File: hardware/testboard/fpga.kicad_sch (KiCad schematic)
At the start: 66 parts, among them J801 Conn_01x06, SW801 Button, U801 SST26VF023BA, U802 SN74ALVC164245, U803 ICE40HX4K-TQ144, U804 SN74ALVC164245, U805 SN74ALVC164245, U806 SN74ALVC164245, U807 SN74ALVC164245, U808 SN74LVC07, U809 74AHCT04, U810 SN74LVC07

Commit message: testboard - schematic and route done
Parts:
- added C1: 4.7uF, Capacitor_SMD:C_0603_1608Metric, symbol Device:C
- added U1: ~, 68040:DACMOD, symbol 68040:DACMOD
- added U2: MAX98306 Amp, 68040:AMP, symbol 68040:AMP
- SW801: value Button -> BUTTON
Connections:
- net +3.3V: now also U810.13, C1.1, U1.1 (VIN), U2.1 (V_{DD})
- net A10: now also U806.23 (2B8); no longer U806.2 (1B1)
- net A11: now also U806.22 (2B7); no longer U806.3 (1B2)
- net A12: now also U806.20 (2B6); no longer U806.5 (1B3)
- net A13: now also U806.19 (2B5); no longer U806.6 (1B4)
- net A14: now also U806.17 (2B4); no longer U806.8 (1B5)
- net A15: now also U806.14 (2B2); no longer U806.11 (1B7)
- net A16: now also U806.16 (2B3); no longer U806.9 (1B6)
- net A17: now also U806.13 (2B1); no longer U806.12 (1B8)
- net A18: now also U806.11 (1B7); no longer U806.14 (2B2)
- net A19: now also U806.12 (1B8); no longer U806.13 (2B1)
- net A20: now also U806.8 (1B5); no longer U806.17 (2B4)
- net A21: now also U806.5 (1B3); no longer U806.20 (2B6)
- net A23: now also U806.9 (1B6); no longer U806.16 (2B3)
- net A25: now also U806.6 (1B4); no longer U806.19 (2B5)
- net A8: now also U806.2 (1B1); no longer U806.23 (2B8)
- net A9: now also U806.3 (1B2); no longer U806.22 (2B7)
- net BCLK: now also U803.94 (IOR_141_GBIN2); no longer U803.20 (IOL_13B_GBIN7)
- net D0: now also U805.6 (1B4); no longer U805.23 (2B8)
- net D1: now also U805.3 (1B2); no longer U805.22 (2B7)
- net D10: now also U805.16 (2B3); no longer U805.9 (1B6)
- net D11: now also U805.17 (2B4); no longer U805.8 (1B5)
- net D12: now also U805.19 (2B5); no longer U805.6 (1B4)
- net D13: now also U805.20 (2B6); no longer U805.5 (1B3)
- net D14: now also U805.22 (2B7); no longer U805.3 (1B2)
- net D15: now also U805.23 (2B8); no longer U805.2 (1B1)
- net D2: now also U805.8 (1B5); no longer U805.20 (2B6)
- net D3: now also U805.2 (1B1); no longer U805.19 (2B5)
- net D4: now also U805.5 (1B3); no longer U805.17 (2B4)
- net D5: now also U805.9 (1B6); no longer U805.16 (2B3)
- net D6: now also U805.11 (1B7); no longer U805.14 (2B2)
- net D7: now also U805.12 (1B8); no longer U805.13 (2B1)
- net D8: now also U805.13 (2B1); no longer U805.12 (1B8)
- net D9: now also U805.14 (2B2); no longer U805.11 (1B7)
- net FPGA_BTN: now also U803.93 (IOR_140_GBIN3); no longer U803.55 (IOB_91)
- net FPGA_LED: now also U803.95 (IOR_144), U808.9; no longer U803.52 (IOB_82_GBIN4), U810.11
- net GND: now also C1.2, U1.2 (GND), U2.2 (GND)
- net LV.A10: now also U803.29 (IOL_23B), U806.26 (2A8); no longer U803.10 (IOL_5B), U806.47 (1A1)
- net LV.A11: now also U803.28 (IOL_23A), U806.27 (2A7); no longer U803.11 (IOL_8A), U806.46 (1A2)
- net LV.A12: now also U803.26 (IOL_18B), U806.29 (2A6); no longer U803.12 (IOL_8B), U806.44 (1A3)
- net LV.A13: now also U803.25 (IOL_18A), U806.30 (2A5); no longer U803.15 (IOL_10A), U806.43 (1A4)
- net LV.A14: now also U803.24 (IOL_17B), U806.32 (2A4); no longer U803.16 (IOL_10B), U806.41 (1A5)
- net LV.A15: now also U803.22 (IOL_14B), U806.35 (2A2); no longer U803.18 (IOL_12B), U806.38 (1A7)
- net LV.A16: now also U803.23 (IOL_17A), U806.33 (2A3); no longer U803.17 (IOL_12A), U806.40 (1A6)
- net LV.A17: now also U803.21 (IOL_14A_GBIN6), U806.36 (2A1); no longer U803.19 (IOL_13A), U806.37 (1A8)
- net LV.A18: now also U803.18 (IOL_12B), U806.38 (1A7); no longer U803.22 (IOL_14B), U806.35 (2A2)
- net LV.A19: now also U803.19 (IOL_13A), U806.37 (1A8); no longer U803.21 (IOL_14A_GBIN6), U806.36 (2A1)
- net LV.A20: now also U803.16 (IOL_10B), U806.41 (1A5); no longer U803.24 (IOL_17B), U806.32 (2A4)
- net LV.A21: now also U803.12 (IOL_8B), U806.44 (1A3); no longer U803.26 (IOL_18B), U806.29 (2A6)
- net LV.A23: now also U803.17 (IOL_12A), U806.40 (1A6); no longer U803.23 (IOL_17A), U806.33 (2A3)
- net LV.A25: now also U803.15 (IOL_10A), U806.43 (1A4); no longer U803.25 (IOL_18A), U806.30 (2A5)
- net LV.A8: now also U803.10 (IOL_5B), U806.47 (1A1); no longer U803.29 (IOL_23B), U806.26 (2A8)
- net LV.A9: now also U803.11 (IOL_8A), U806.46 (1A2); no longer U803.28 (IOL_23A), U806.27 (2A7)
- net LV_68150_CS: now also U803.104 (IOR_164); no longer U803.44 (IOB_72)
- net LV_AVEC: now also U803.107 (IOR_167); no longer U803.42 (IOB_64)
- net LV_COM_CS: now also U803.102 (IOR_161); no longer U803.43 (IOB_71)
- net LV_COM_IACK: now also U803.105 (IOR_165); no longer U803.39 (IOB_61)
- net LV_D0: now also U803.138 (IOT_216), U805.43 (1A4); no longer U803.9 (IOL_5A), U805.26 (2A8)
- net LV_D1: now also U803.136 (IOT_214), U805.46 (1A2); no longer U803.8 (IOL_4B), U805.27 (2A7)
- net LV_D10: now also U803.2 (IOL_2B), U805.33 (2A3); no longer U803.141 (IOT_219), U805.40 (1A6)
- net LV_D11: now also U803.3 (IOL_3A), U805.32 (2A4); no longer U803.139 (IOT_217), U805.41 (1A5)
- net LV_D12: now also U803.4 (IOL_3B), U805.30 (2A5); no longer U803.138 (IOT_216), U805.43 (1A4)
- net LV_D13: now also U803.7 (IOL_4A), U805.29 (2A6); no longer U803.137 (IOT_215), U805.44 (1A3)
- net LV_D14: now also U803.8 (IOL_4B), U805.27 (2A7); no longer U803.136 (IOT_214), U805.46 (1A2)
- net LV_D15: now also U803.9 (IOL_5A), U805.26 (2A8); no longer U803.135 (IOT_213), U805.47 (1A1)
- net LV_D2: now also U803.139 (IOT_217), U805.41 (1A5); no longer U803.7 (IOL_4A), U805.29 (2A6)
- net LV_D3: now also U803.135 (IOT_213), U805.47 (1A1); no longer U803.4 (IOL_3B), U805.30 (2A5)
- net LV_D4: now also U803.137 (IOT_215), U805.44 (1A3); no longer U803.3 (IOL_3A), U805.32 (2A4)
- net LV_D5: now also U803.141 (IOT_219), U805.40 (1A6); no longer U803.2 (IOL_2B), U805.33 (2A3)
- net LV_D6: now also U803.142 (IOT_220), U805.38 (1A7); no longer U803.1 (IOL_2A), U805.35 (2A2)
- net LV_D7: now also U803.143 (IOT_221), U805.37 (1A8); no longer U803.144 (IOT_222), U805.36 (2A1)
- net LV_D8: now also U803.144 (IOT_222), U805.36 (2A1); no longer U803.143 (IOT_221), U805.37 (1A8)
- net LV_D9: now also U803.1 (IOL_2A), U805.35 (2A2); no longer U803.142 (IOT_220), U805.38 (1A7)
- net LV_RAM_CS: now also U803.106 (IOR_166); no longer U803.41 (IOB_63)
- net LV_R/~{W}: now also U803.42 (IOB_64)
- net LV_SIZ0: now also U803.43 (IOB_71)
- net LV_SIZ1: now also U803.44 (IOB_72)
- net LV_TM0: now also U803.41 (IOB_63)
- net LV_TM1: now also U803.39 (IOB_61)
- net LV_TM2: now also U803.38 (IOB_57)
- net LV_TT0: now also U803.49 (IOB_81_GBIN5)
- net LV_TT1: now also U803.48 (IOB_80)
- net LV_~{68150_DS}: now also U803.56 (IOB_94)
- net LV_~{COM_IRQ}: now also U802.29 (2A6), U803.55 (IOB_91); no longer U802.33 (2A3)
- net LV_~{DSACK0}: now also U803.96 (IOR_146), U808.11; no longer U803.101 (IOR_160), U808.9
- net LV_~{DSACK1}: now also U803.97 (IOR_147), U808.13; no longer U803.102 (IOR_161), U808.11
- net LV_~{IPL0}: now also U803.98 (IOR_148); no longer U803.105 (IOR_165)
- net LV_~{IPL1}: now also U803.99 (IOR_152); no longer U803.106 (IOR_166)
- net LV_~{IPL2}: now also U803.101 (IOR_160); no longer U803.107 (IOR_167)
- net LV_~{RST}: now also U802.27 (2A7), U803.52 (IOB_82_GBIN4); no longer U802.30 (2A5), U803.48 (IOB_80)
- net LV_~{TA}: now also U803.34 (IOL_25B), U810.11; no longer U803.104 (IOR_164), U808.13
- net LV_~{TBI}: now also U803.31 (IOL_24A)
- net LV_~{TCI}: now also U803.32 (IOL_24B)
- net LV_~{TEA}: now also U803.33 (IOL_25A)
- net LV_~{TIP}: now also U803.47 (IOB_79)
- net LV_~{TS}: now also U803.45 (IOB_73)
- net ~{COM_IRQ}: now also U802.20 (2B6); no longer U802.16 (2B3)
- net ~{DSACK0}: now also U808.10; no longer U808.8
- net ~{DSACK1}: now also U808.12; no longer U808.10
- net ~{RST}: now also U802.22 (2B7); no longer U802.19 (2B5)
- net ~{TA}: now also U810.10; no longer U808.12
- net at D803.1 (K): now also U808.8; no longer U810.10
- net SND_BCLK: now reaches U803.60 (IOB_95)
- net SND_BCLK: now also U1.5 (BCK)
- net SND_DOUT: now reaches U803.61 (IOB_96)
- net SND_DOUT: now also U1.4 (DIN)
- net SND_LRCLK: now reaches U803.62 (IOB_102)
- net SND_LRCLK: now also U1.3 (LRCLK)
- net ~{FPGA_RDY} renamed ~{FPGA_WAIT}
- new net: U1.10 (G), U2.7 (R-)
- new net: U1.7 (L), U2.4 (L+)
- new net: U1.8 (G), U2.5 (L-)
- new net: U1.9 (R), U2.6 (R+)
- no-connect marks 2 -> 13
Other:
- note removed: "From VCCIO_2"
- moved on the sheet: C801, C804, C806, C808, C809, C810, C811, C812, C813, C814, C815, C817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

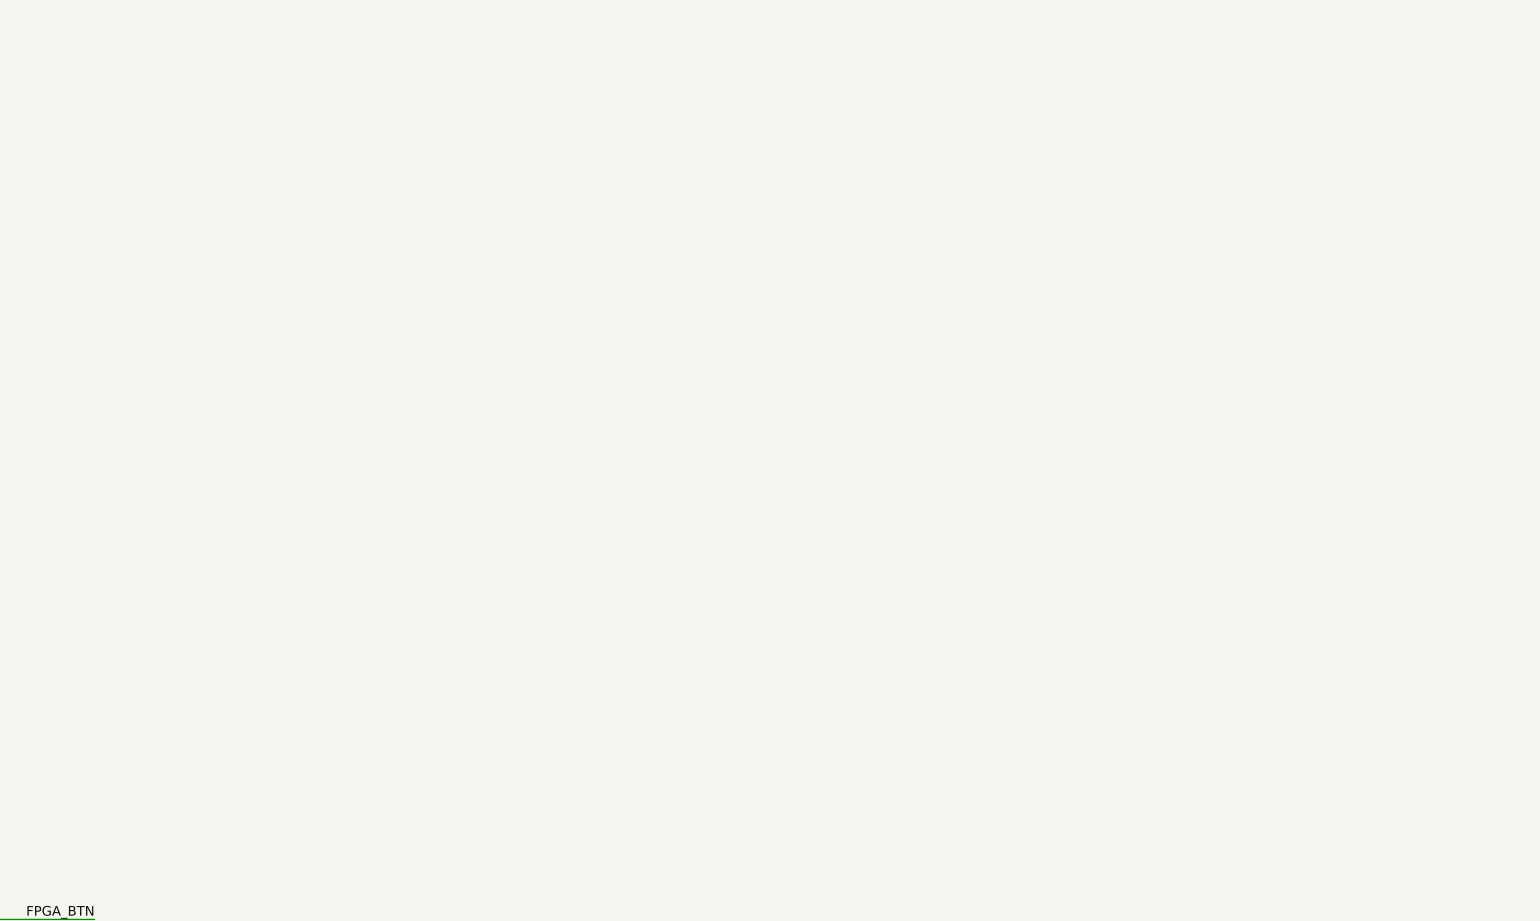
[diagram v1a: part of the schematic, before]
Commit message: make 3.3v reg bigger
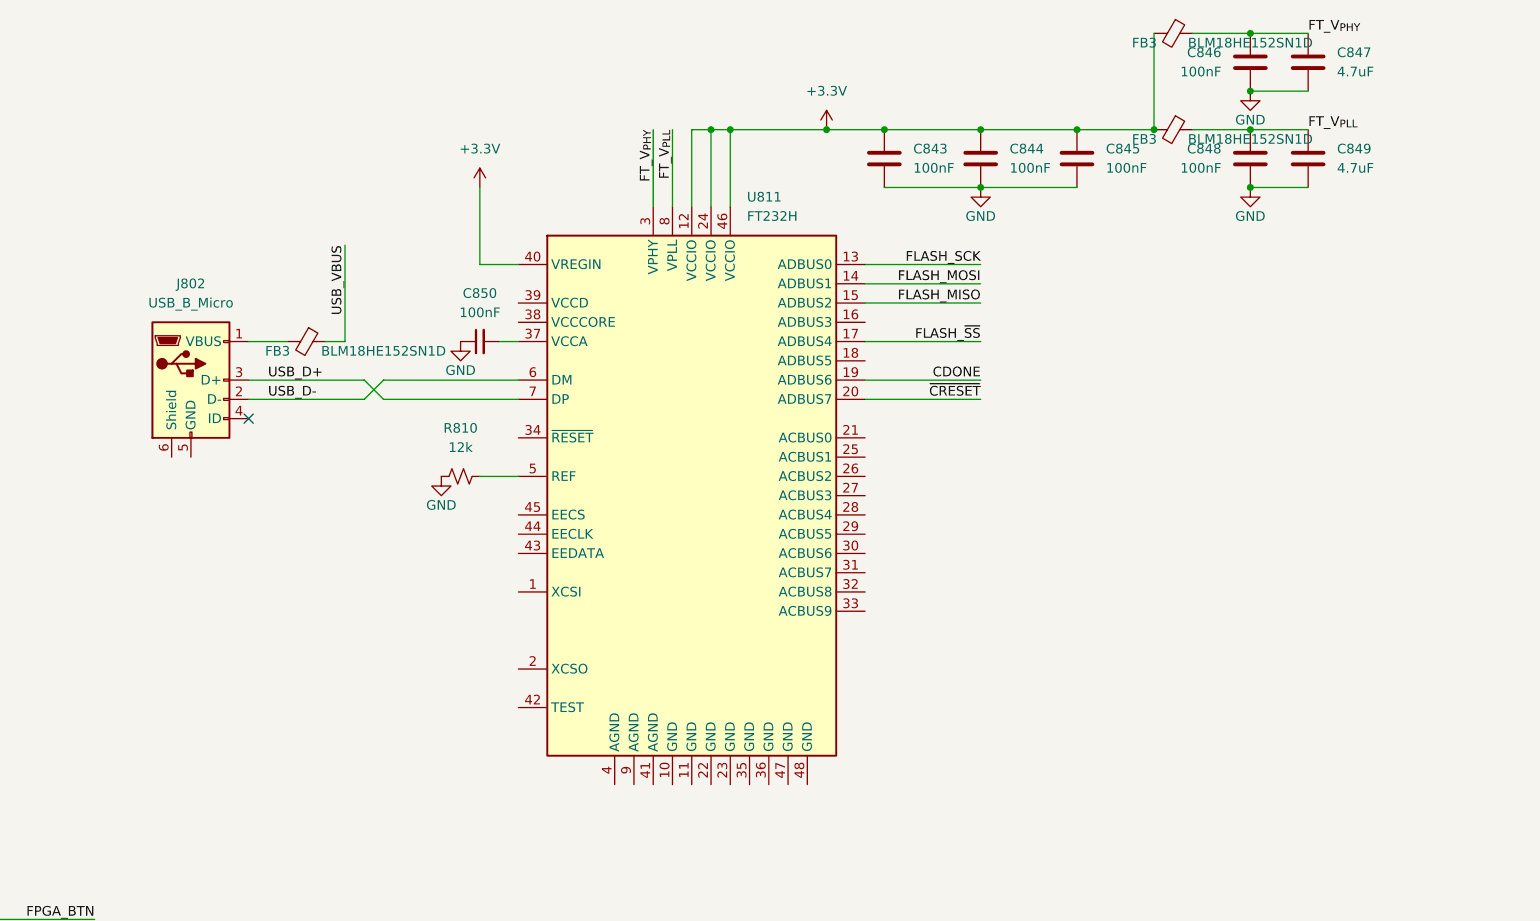
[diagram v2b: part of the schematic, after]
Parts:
- added C843, C844, C845, C846, C848: 100nF, symbol Device:C
- added C847, C849: 4.7uF, symbol Device:C
- added C850: 100nF, symbol Device:C_Small
- added FB3 (x3): BLM18HE152SN1D, Inductor_SMD:L_0603_1608Metric, symbol Device:FerriteBead_Small
- added J802: USB_B_Micro, Connector_USB:USB_Micro-AB_Molex_47590-0001, symbol Connector:USB_B_Micro
- added R810: 12k, symbol Device:R_Small_US
- added U811: FT232H, Package_DFN_QFN:QFN-48-1EP_8x8mm_P0.5mm_EP6.2x6.2mm, symbol Interface_USB:FT232H
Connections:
- net +3.3V: now also C843.1, C844.1, C845.1, FB3.2, FB3.2, U811.12 (VCCIO), U811.24 (VCCIO), U811.40 (VREGIN), U811.46 (VCCIO)
- net CDONE: now also U811.19 (ADBUS6)
- net FLASH_MISO: now also U811.15 (ADBUS2)
- net FLASH_MOSI: now also U811.14 (ADBUS1)
- net FLASH_SCK: now also U811.13 (ADBUS0)
- net GND: now also C843.2, C844.2, C845.2, C846.2, C847.2, C848.2, C849.2, C850.1, R810.1
- new net: C850.2, U811.37 (VCCA)
- new net: FB3.2, J802.1 (VBUS)
- new net: R810.2, U811.5 (REF)
- new net FLASH_~{SS}: U811.17 (ADBUS4)
- new net FT_V_{PHY}: C846.1, C847.1, FB3.1, U811.3 (VPHY)
- new net FT_V_{PLL}: C848.1, C849.1, FB3.1, U811.8 (VPLL)
- new net USB_D+: J802.3 (D+), U811.7 (DP)
- new net USB_D-: J802.2 (D-), U811.6 (DM)
- new net USB_VBUS: FB3.1
- new net ~{CRESET}: U811.20 (ADBUS7)
- no-connect marks 13 -> 14

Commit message: layout FTDI
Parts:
- removed D802: D_Schottky, Diode_SMD:D_0603_1608Metric, symbol Device:D_Schottky
- removed J801: Conn_01x06, Connector_JST:JST_PH_B6B-PH-K_1x06_P2.00mm_Vertical, symbol Connector_Generic:Conn_01x06
- added C2, C3: 10nF, Capacitor_SMD:C_0603_1608Metric, symbol Device:C_Small
- added C4, C5: 27pF, Capacitor_SMD:C_0603_1608Metric, symbol Device:C_Small
- added D1, D2: PGB1010603, Diode_SMD:D_0603_1608Metric, symbol Device:D_TVS
- added R1, R2, R4, R5: 10k, Resistor_SMD:R_0603_1608Metric, symbol Device:R_Small_US
- added R3: 39k, Resistor_SMD:R_0603_1608Metric, symbol Device:R_Small_US
- added R6: 2k, Resistor_SMD:R_0603_1608Metric, symbol Device:R_Small_US
- added U3: 93LCxxBxxOT, Package_TO_SOT_SMD:SOT-23-6, symbol Memory_EEPROM:93LCxxBxxOT
- added Y1: 12MHz, Crystal:Crystal_SMD_Abracon_ABM8G-4Pin_3.2x2.5mm, symbol Device:Crystal_GND24
- C843, C844, C845, C846, C848, C850: footprint (none) -> Capacitor_SMD:C_0603_1608Metric
- C847, C849: footprint (none) -> Capacitor_SMD:C_0603_1608Metric; now not fitted
- R810: footprint (none) -> Resistor_SMD:R_0603_1608Metric
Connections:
- net FLASH_POWER is gone; now on net +3.3V: C801.1, R803.2, R804.2, U801.8 (VCC)
- net FLASH_~{SS} is gone; now on net FLASH_SS: U811.17 (ADBUS4)
- net +3.3V: now also U811.39 (VCCD), C3.2, R1.2, R2.1, R4.1, R5.1, U3.6 (VCC)
- net GND: now also J802.5 (GND), J802.6 (Shield), U811.10 (GND), U811.11 (GND), U811.22 (GND), U811.23 (GND), U811.35 (GND), U811.36 (GND), U811.4 (AGND), U811.41 (AGND), U811.42 (TEST), U811.47 (GND), U811.48 (GND), U811.9 (AGND), C2.1, C3.1, C4.1, C5.1, D1.1 (A1), D2.1 (A1), U3.2 (GND), Y1.2, Y1.4
- net USB_D+: now also D2.2 (A2)
- net USB_D-: now also D1.2 (A2)
- net USB_VBUS: now also C2.2, R3.2
- net at U811.1 (XCSI): now also C4.2, Y1.1
- net at U811.2 (XCSO): now also C5.2, Y1.3
- net at U811.31 (ACBUS7): now also R3.1
- net at U811.34 (~{RESET}): now also R1.1
- net FTDI_VCORE: now reaches U811.38 (VCCCORE)
- net FTDI_F_DATA: now reaches U811.43 (EEDATA)
- net FTDI_F_DATA: now also R4.2, R6.2, U3.3 (DI)
- net FTDI_F_CLK: now reaches U811.44 (EECLK)
- net FTDI_F_CLK: now also R2.2, U3.4 (CLK)
- net FTDI_F_~{CS}: now reaches U811.45 (EECS)
- net FTDI_F_~{CS}: now also R5.2, U3.5 (CS)
- new net: R6.1, U3.1 (DO)
- no-connect marks 14 -> 25
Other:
- moved on the sheet: C843, C844, C845, C846, C848, FB3, J802, R810

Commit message: finish routing testboard
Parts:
- J802: footprint Connector_USB:USB_Micro-AB_Molex_47590-0001 -> Connector_USB:USB_Micro-B_Amphenol_10104110_Horizontal
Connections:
- net ~{CRESET}: now also R805.2, U803.66 (~{CRESET})
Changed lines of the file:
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@@
     (stroke (width 0) (type default))
   )
+  (wire (pts (xy 137.16 276.86) (xy 157.48 276.86))
+    (stroke (width 0) (type default))
+  )
   (wire (pts (xy 157.48 264.16) (xy 144.78 264.16))
     (stroke (width 0) (type default))
@@
     (stroke (width 0) (type default))
   )
-  (wire (pts (xy 157.48 276.86) (xy 137.16 276.86))
-    (stroke (width 0) (type default))
-  )
   (bus (pts (xy 231.14 579.12) (xy 231.14 581.66))
     (stroke (width 0) (type default))
@@
     (effects (font (size 1.27 1.27)) (justify left bottom))
   )
+  (label "~{CRESET}" (at 137.16 276.86 0) (fields_autoplaced)
+    (effects (font (size 1.27 1.27)) (justify left bottom))
+  )
   (label "LV.A17" (at 289.56 510.54 180) (fields_autoplaced)
     (effects (font (size 1.27 1.27)) (justify right bottom))
@@
       (effects (font (size 1.27 1.27)))
     )
-    (property "Footprint" "Connector_USB:USB_Micro-AB_Molex_47590-0001" (at 87.63 123.19 0)
+    (property "Footprint" "Connector_USB:USB_Micro-B_Amphenol_10104110_Horizontal" (at 87.63 123.19 0)
       (effects (font (size 1.27 1.27)) hide)
     )

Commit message: remove duplicate LV_A0 track
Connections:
- net LV.A0: no longer U803.37 (IOB_56)
- no-connect marks 25 -> 26
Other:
- note added: "//TODO: Fix this ugly schematic layout"
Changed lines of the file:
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@@
   (no_connect (at 187.96 119.38))
   (no_connect (at 187.96 132.08))
+  (no_connect (at 439.42 152.4))
   (no_connect (at 101.6 520.7))
   (no_connect (at 480.06 482.6))
@@
     (stroke (width 0) (type default))
   )
-  (wire (pts (xy 429.26 152.4) (xy 439.42 152.4))
-    (stroke (width 0) (type default))
-  )
   (wire (pts (xy 99.06 622.3) (xy 96.52 622.3))
     (stroke (width 0) (type default))
@@
     (stroke (width 0) (type default))
   )
+  (text "//TODO: Fix this ugly schematic layout" (at 88.9 177.8 0)
+    (effects (font (size 1.27 1.27)) (justify left bottom))
+  )
   (text "V_{CC} at 27, 40, 92, 111" (at 160.02 294.64 0)
     (effects (font (size 1.27 1.27)) (justify right bottom))
@@
     (effects (font (size 1.27 1.27)) (justify left bottom))
   )
-  (label "LV.A0" (at 429.26 152.4 0) (fields_autoplaced)
-    (effects (font (size 1.27 1.27)) (justify left bottom))
-  )

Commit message: Gerbers published, board out for production!
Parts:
- J802: footprint Connector_USB:USB_Micro-B_Amphenol_10104110_Horizontal -> Connector_USB:USB_Micro-B_Amphenol_10118193-0001LF_Horizontal
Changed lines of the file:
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@@
       (effects (font (size 1.27 1.27)))
     )
-    (property "Footprint" "Connector_USB:USB_Micro-B_Amphenol_10104110_Horizontal" (at 87.63 123.19 0)
+    (property "Footprint" "Connector_USB:USB_Micro-B_Amphenol_10118193-0001LF_Horizontal" (at 87.63 123.19 0)
       (effects (font (size 1.27 1.27)) hide)
     )

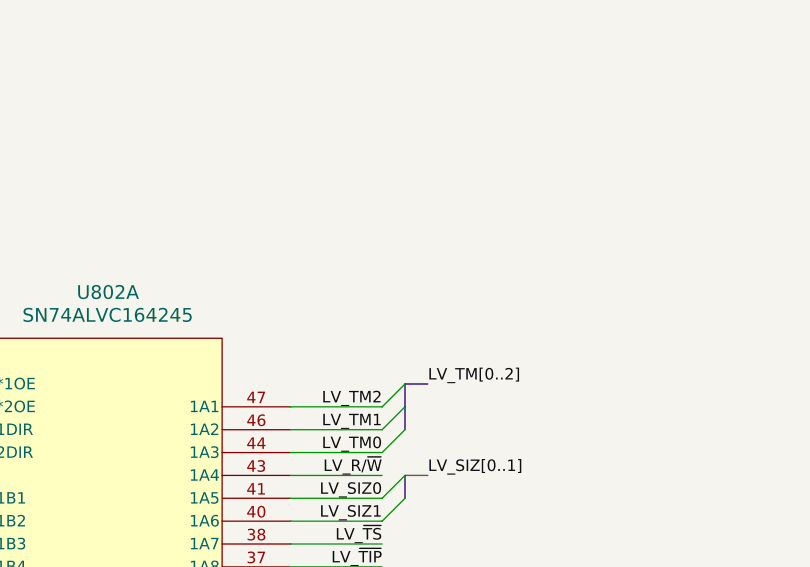
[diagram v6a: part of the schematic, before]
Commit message: update errata for testboard
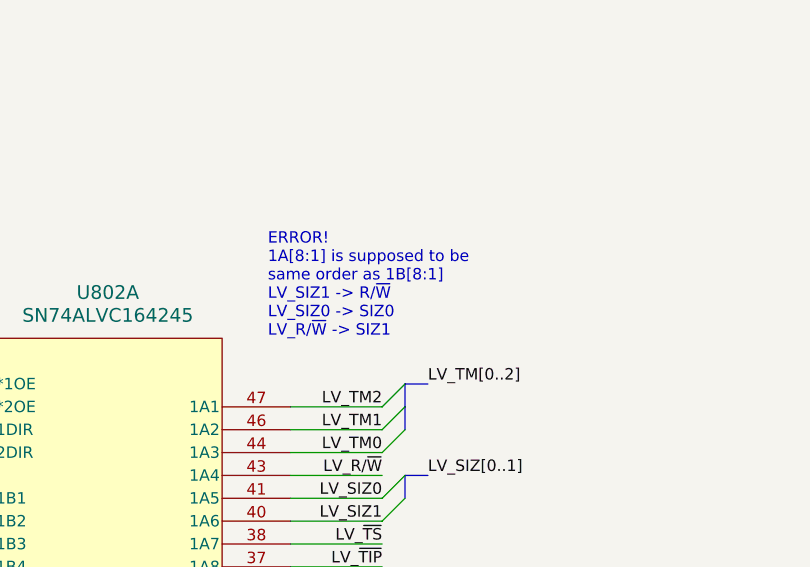
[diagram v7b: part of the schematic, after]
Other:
- note added: "ERROR! 1A[8:1] is supposed to be same order as 1B[8:1] LV_SIZ1 -> R/~{W} LV_SIZ0 -> SIZ0 LV_R/~{W} -> SIZ1"
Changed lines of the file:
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@@
+    (effects (font (size 1.27 1.27)) (justify left bottom))
+  )
+  (text "ERROR!\n1A[8:1] is supposed to be\nsame order as 1B[8:1]\nLV_SIZ1 -> R/~{W}\nLV_SIZ0 -> SIZ0\nLV_R/~{W} -> SIZ1"
+    (at 139.7 474.98 0)
     (effects (font (size 1.27 1.27)) (justify left bottom))
   )
